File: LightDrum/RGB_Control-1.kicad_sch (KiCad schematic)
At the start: 25 parts, among them Q301 PMXB43UNEZ, Q302 PMXB43UNEZ, Q303 PMXB43UNEZ, Q304 PMXB43UNEZ, Q305 PMXB43UNEZ, Q306 PMXB43UNEZ, Q307 PMXB43UNEZ, Q308 PMXB43UNEZ, U301 PCA9634_TSSOP20

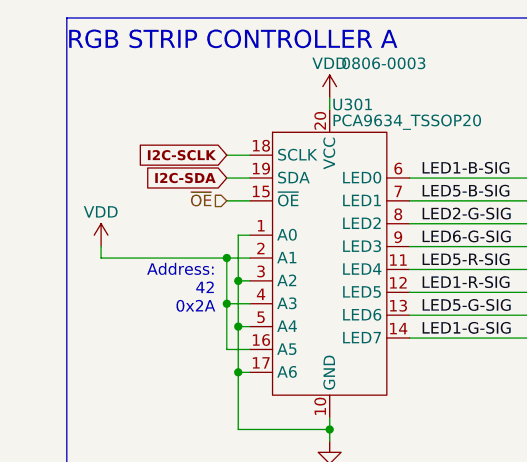
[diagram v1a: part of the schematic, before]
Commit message: Preliminary schematic lock - Starting PCB layout
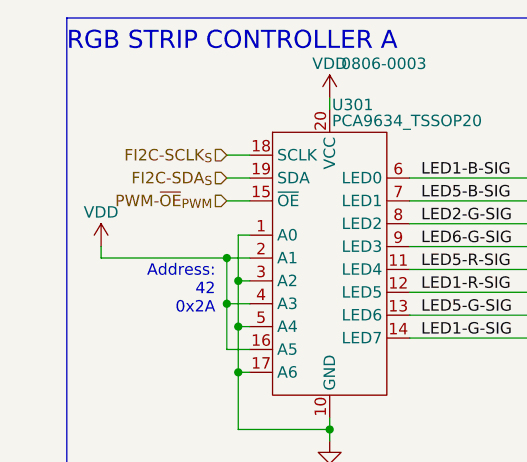
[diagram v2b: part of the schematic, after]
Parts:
- Q301, Q302, Q303, Q304, Q305, Q306, Q307, Q308: SupplierPN (none) -> 1727-PMXB43UNEZCT-ND
- R301, R302, R303, R304, R309, R310, R311, R312: SupplierPN (none) -> RMCF0402FT100RCT-ND
- R305, R306, R307, R308, R313, R314, R315, R316: SupplierPN (none) -> 311-10KJRCT-ND
- U301: SupplierPN (none) -> 568-4066-1-ND
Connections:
- net I2C-SCLK renamed FI2C-SCLK_{S}
- net I2C-SDA renamed FI2C-SDA_{S}
- net ~{OE} renamed PWM-~{OE}_{PWM}
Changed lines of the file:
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@@
   (title_block
     (title "LightDrum")
-    (rev "REV10")
+    (rev "REV11")
     (company "Daxxn Industries")
   )
@@
     (effects (font (size 1.27 1.27)) (justify left bottom))
   )
-  (global_label "I2C-SCLK" (shape input) (at 34.29 31.75 180) (fields_autoplaced)
-    (effects (font (size 1.1 1.1) (thickness 0.254) bold) (justify right))
-    (property "Intersheetrefs" "${INTERSHEET_REFS}" (at 23.7956 31.623 0)
-      (effects (font (size 1.1 1.1) (thickness 0.254) bold) (justify right) hide)
-    )
-  )
-  (global_label "I2C-SDA" (shape input) (at 34.29 34.29 180) (fields_autoplaced)
-    (effects (font (size 1.1 1.1) (thickness 0.254) bold) (justify right))
-    (property "Intersheetrefs" "${INTERSHEET_REFS}" (at 24.8432 34.163 0)
-      (effects (font (size 1.1 1.1) (thickness 0.254) bold) (justify right) hide)
-    )
+  (hierarchical_label "FI2C-SCLK_{S}" (shape input) (at 34.29 31.75 180) (fields_autoplaced)
+    (effects (font (size 1.27 1.27)) (justify right))
   )
   (hierarchical_label "LED5-R" (shape output) (at 102.87 46.99 0) (fields_autoplaced)
     (effects (font (size 1.27 1.27)) (justify left))
   )
+  (hierarchical_label "FI2C-SDA_{S}" (shape input) (at 34.29 34.29 180) (fields_autoplaced)
+    (effects (font (size 1.27 1.27)) (justify right))
+  )
   (hierarchical_label "LED5-G" (shape output) (at 153.67 46.99 0) (fields_autoplaced)
     (effects (font (size 1.27 1.27)) (justify left))
@@
     (effects (font (size 1.27 1.27)) (justify left))
   )
-  (hierarchical_label "~{OE}" (shape input) (at 34.29 36.83 180) (fields_autoplaced)
+  (hierarchical_label "PWM-~{OE}_{PWM}" (shape input) (at 34.29 36.83 180) (fields_autoplaced)
     (effects (font (size 1.27 1.27)) (justify right))
   )
@@
       (effects (font (size 1.27 1.27)) (justify left))
     )
+    (property "SupplierPN" "1727-PMXB43UNEZCT-ND" (at 138.43 76.2 0)
+      (effects (font (size 1.27 1.27)) hide)
+    )
     (pin "1")
     (pin "2")
@@
       (effects (font (size 1.27 1.27)) hide)
     )
+    (property "SupplierPN" "RMCF0402FT100RCT-ND" (at 109.22 72.39 0)
+      (effects (font (size 1.27 1.27)) hide)
+    )
     (pin "1")
     (pin "2")
@@
       (effects (font (size 1.27 1.27)) (justify left))
     )
+    (property "SupplierPN" "1727-PMXB43UNEZCT-ND" (at 125.73 52.07 0)
+      (effects (font (size 1.27 1.27)) hide)
+    )
     (pin "1")
     (pin "2")
@@
       (effects (font (size 1.27 1.27)) hide)
     )
+    (property "SupplierPN" "RMCF0402FT100RCT-ND" (at 185.42 72.39 0)
+      (effects (font (size 1.27 1.27)) hide)
+    )
     (pin "1")
     (pin "2")
@@
       (effects (font (size 1.27 1.27)) hide)
     )
+    (property "SupplierPN" "311-10KJRCT-ND" (at 172.72 55.88 0)
+      (effects (font (size 1.27 1.27)) hide)
+    )
     (pin "1")
     (pin "2")
@@
       (effects (font (size 1.27 1.27)) hide)
     )
+    (property "SupplierPN" "311-10KJRCT-ND" (at 109.22 80.01 0)
+      (effects (font (size 1.27 1.27)) hide)
+    )
     (pin "1")
     (pin "2")
@@
       (effects (font (size 1.27 1.27)) hide)
     )
+    (property "SupplierPN" "RMCF0402FT100RCT-ND" (at 172.72 48.26 0)
+      (effects (font (size 1.27 1.27)) hide)
+    )
     (pin "1")
     (pin "2")
@@
       (effects (font (size 1.27 1.27)) hide)
     )
+    (property "SupplierPN" "311-10KJRCT-ND" (at 121.92 55.88 0)
+      (effects (font (size 1.27 1.27)) hide)
+    )
     (pin "1")
     (pin "2")
@@
       (effects (font (size 1.27 1.27)) hide)
     )
+    (property "SupplierPN" "311-10KJRCT-ND" (at 134.62 80.01 0)
+      (effects (font (size 1.27 1.27)) hide)
+    )
     (pin "1")
     (pin "2")
@@
       (effects (font (size 1.27 1.27)) (justify left))
     )
+    (property "SupplierPN" "1727-PMXB43UNEZCT-ND" (at 113.03 76.2 0)
+      (effects (font (size 1.27 1.27)) hide)
+    )
     (pin "1")
     (pin "2")
@@
     )
     (property "Datasheet" "~" (at 160.02 80.01 0)
+      (effects (font (size 1.27 1.27)) hide)
+    )
+    (property "SupplierPN" "311-10KJRCT-ND" (at 160.02 80.01 0)
       (effects (font (size 1.27 1.27)) hide)
     )
@@
       (effects (font (size 1.27 1.27)) hide)
     )
+    (property "SupplierPN" "RMCF0402FT100RCT-ND" (at 160.02 72.39 0)
+      (effects (font (size 1.27 1.27)) hide)
+    )
     (pin "1")
     (pin "2")
@@
       (effects (font (size 1.27 1.27)) hide)
     )
+    (property "SupplierPN" "RMCF0402FT100RCT-ND" (at 121.92 48.26 0)
+      (effects (font (size 1.27 1.27)) hide)
+    )
     (pin "1")
     (pin "2")
@@
     (property "PartNumber" "0703-0003" (at 102.87 48.26 0)
       (effects (font (size 1.27 1.27)) (justify left))
+    )
+    (property "SupplierPN" "1727-PMXB43UNEZCT-ND" (at 100.33 52.07 0)
+      (effects (font (size 1.27 1.27)) hide)
     )
     (pin "1")
@@
       (effects (font (size 1.27 1.27)) (justify left))
     )
+    (property "SupplierPN" "1727-PMXB43UNEZCT-ND" (at 163.83 76.2 0)
+      (effects (font (size 1.27 1.27)) hide)
+    )
     (pin "1")
     (pin "2")
@@
       (effects (font (size 1.27 1.27)) hide)
     )
+    (property "SupplierPN" "RMCF0402FT100RCT-ND" (at 96.52 48.26 0)
+      (effects (font (size 1.27 1.27)) hide)
+    )
     (pin "1")
     (pin "2")
@@
       (effects (font (size 1.27 1.27)) hide)
     )
+    (property "SupplierPN" "311-10KJRCT-ND" (at 96.52 55.88 0)
+      (effects (font (size 1.27 1.27)) hide)
+    )
     (pin "1")
     (pin "2")
@@
       (effects (font (size 1.27 1.27)) hide)
     )
+    (property "SupplierPN" "311-10KJRCT-ND" (at 185.42 80.01 0)
+      (effects (font (size 1.27 1.27)) hide)
+    )
     (pin "1")
     (pin "2")
@@
       (effects (font (size 1.27 1.27)) hide)
     )
+    (property "SupplierPN" "311-10KJRCT-ND" (at 147.32 55.88 0)
+      (effects (font (size 1.27 1.27)) hide)
+    )
     (pin "1")
     (pin "2")
@@
     (property "PartNumber" "0806-0003" (at 46.99 21.59 0)
       (effects (font (size 1.27 1.27)) (justify left))
+    )
+    (property "SupplierPN" "568-4066-1-ND" (at 45.72 43.18 0)
+      (effects (font (size 1.27 1.27)) hide)
     )
     (pin "1")
@@
       (effects (font (size 1.27 1.27)) hide)
     )
+    (property "SupplierPN" "RMCF0402FT100RCT-ND" (at 134.62 72.39 0)
+      (effects (font (size 1.27 1.27)) hide)
+    )
     (pin "1")
     (pin "2")
@@
       (effects (font (size 1.27 1.27)) (justify left))
     )
+    (property "SupplierPN" "1727-PMXB43UNEZCT-ND" (at 189.23 76.2 0)
+      (effects (font (size 1.27 1.27)) hide)
+    )
     (pin "1")
     (pin "2")
@@
       (effects (font (size 1.27 1.27)) hide)
     )
+    (property "SupplierPN" "RMCF0402FT100RCT-ND" (at 147.32 48.26 0)
+      (effects (font (size 1.27 1.27)) hide)
+    )
     (pin "1")
     (pin "2")
@@
       (effects (font (size 1.27 1.27)) (justify left))
     )
+    (property "SupplierPN" "1727-PMXB43UNEZCT-ND" (at 151.13 52.07 0)
+      (effects (font (size 1.27 1.27)) hide)
+    )
     (pin "1")
     (pin "2")
@@
       (effects (font (size 1.27 1.27)) (justify left))
     )
-    (pin "1")
+    (property "SupplierPN" "1727-PMXB43UNEZCT-ND" (at 176.53 52.07 0)
+      (effects (font (size 1.27 1.27)) hide)
+    )
+    (pin "1")

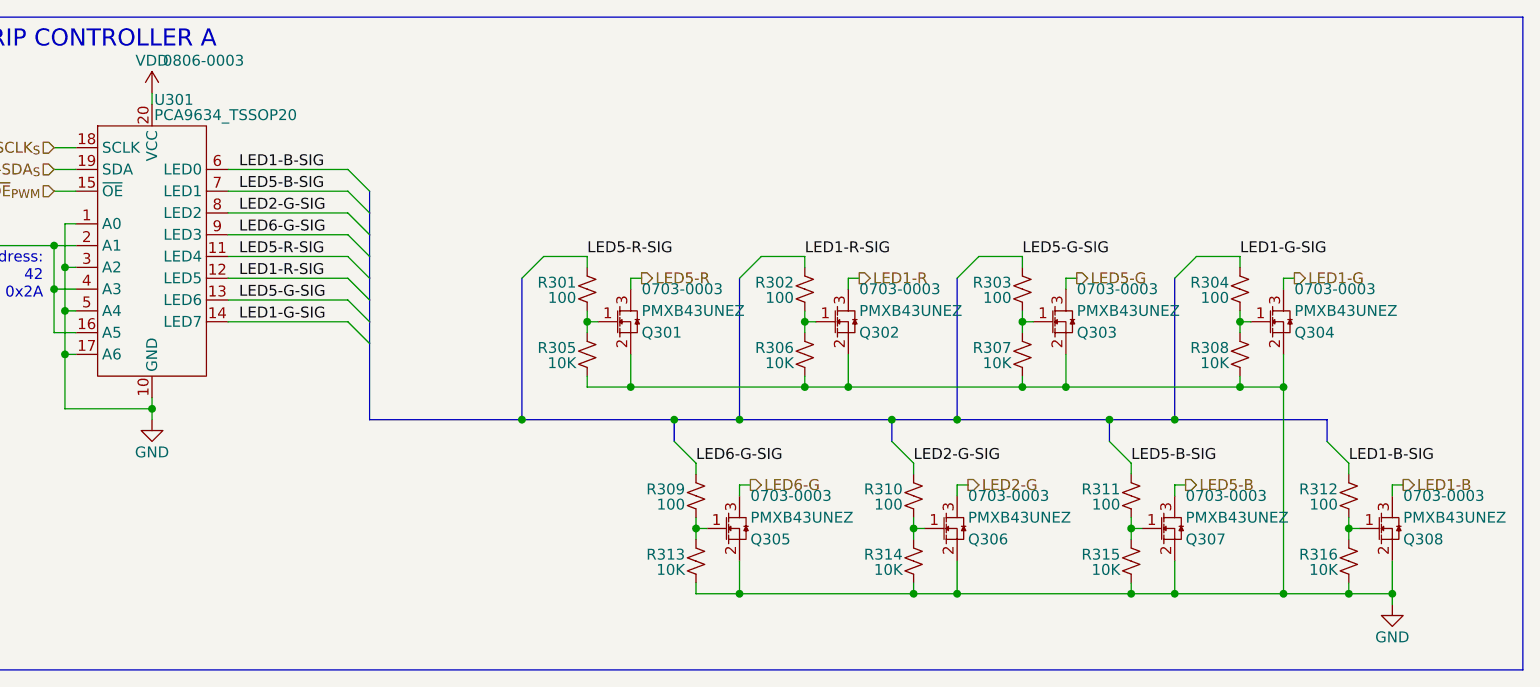
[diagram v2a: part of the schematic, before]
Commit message: Component placement complete
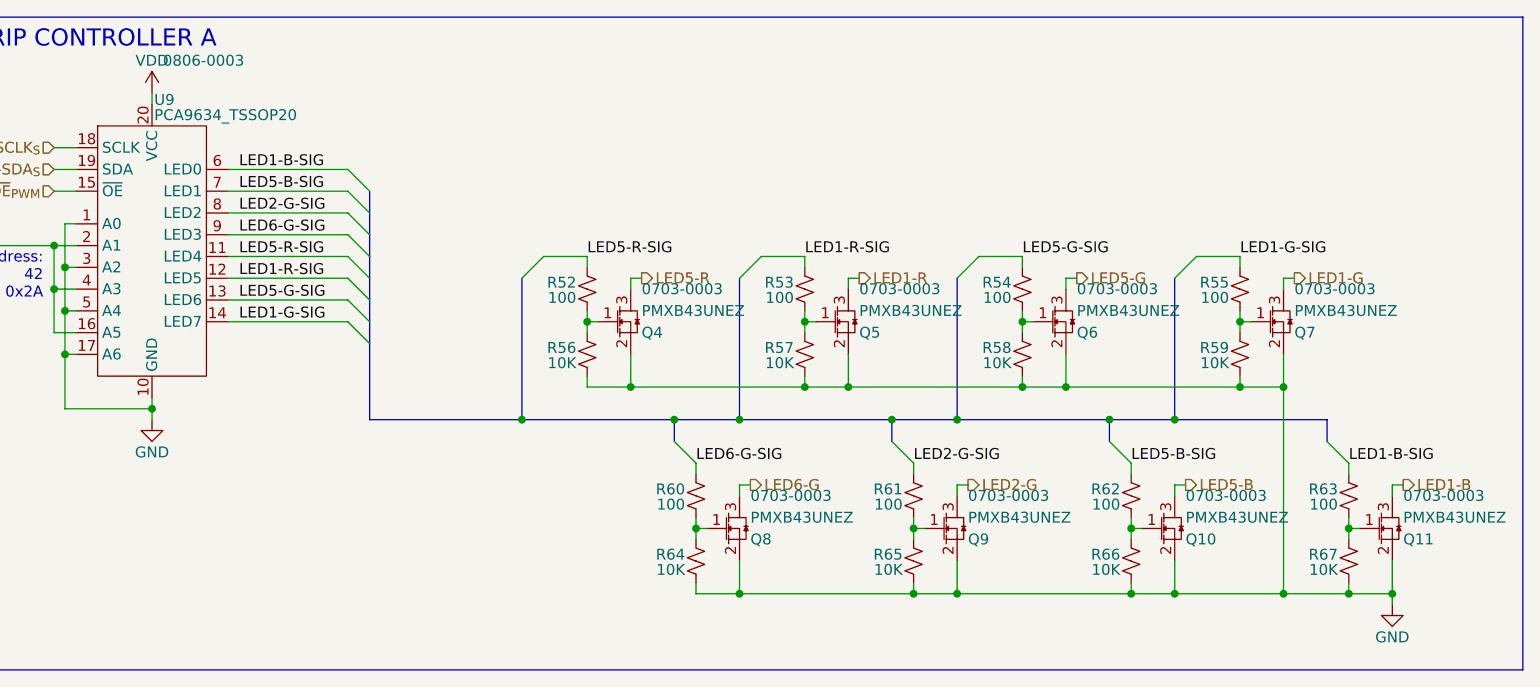
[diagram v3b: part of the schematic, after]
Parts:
- renumbered Q307 to Q10, Q308 to Q11, Q301 to Q4, Q302 to Q5, Q303 to Q6, Q304 to Q7, Q305 to Q8, Q306 to Q9, R301 to R52, R302 to R53, R303 to R54, R304 to R55, R305 to R56, R306 to R57, R307 to R58, R308 to R59, R309 to R60, R310 to R61, R311 to R62, R312 to R63, R313 to R64, R314 to R65, R315 to R66, R316 to R67, U301 to U9

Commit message: First draft layout almost complete
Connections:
- net LED1-B-SIG: now also U9.9 (LED3); no longer U9.6 (LED0)
- net LED2-G-SIG: now also U9.7 (LED1); no longer U9.8 (LED2)
- net LED5-B-SIG: now also U9.8 (LED2); no longer U9.7 (LED1)
- net LED6-G-SIG: now also U9.6 (LED0); no longer U9.9 (LED3)
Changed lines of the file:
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@@
     (effects (font (size 1.27 1.27)) (justify left bottom))
   )
-  (label "LED1-B-SIG" (at 55.88 34.29 0) (fields_autoplaced)
+  (label "LED1-B-SIG" (at 55.88 41.91 0) (fields_autoplaced)
     (effects (font (size 1.27 1.27)) (justify left bottom))
   )
@@
     (effects (font (size 1.27 1.27)) (justify left bottom))
   )
-  (label "LED5-B-SIG" (at 55.88 36.83 0) (fields_autoplaced)
+  (label "LED5-B-SIG" (at 55.88 39.37 0) (fields_autoplaced)
     (effects (font (size 1.27 1.27)) (justify left bottom))
   )
-  (label "LED2-G-SIG" (at 55.88 39.37 0) (fields_autoplaced)
+  (label "LED2-G-SIG" (at 55.88 36.83 0) (fields_autoplaced)
     (effects (font (size 1.27 1.27)) (justify left bottom))
   )
@@
     (effects (font (size 1.27 1.27)) (justify left bottom))
   )
-  (label "LED6-G-SIG" (at 55.88 41.91 0) (fields_autoplaced)
+  (label "LED6-G-SIG" (at 55.88 34.29 0) (fields_autoplaced)
     (effects (font (size 1.27 1.27)) (justify left bottom))
   )

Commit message: Minor fixes and cleanup - REV11
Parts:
- added C75, C76: 100nF, Capacitor_SMD:C_0402_1005Metric, symbol Daxxn_Device:C
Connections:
- net GND: now also C75.2, C76.2
- net VDD: now also C75.1, C76.1
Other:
- moved on the sheet: Q10, Q11, Q4, Q5, Q6, Q7, Q8, Q9, R52, R53, R54, R55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
